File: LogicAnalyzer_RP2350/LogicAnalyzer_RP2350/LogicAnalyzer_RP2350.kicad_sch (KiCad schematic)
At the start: 0 parts

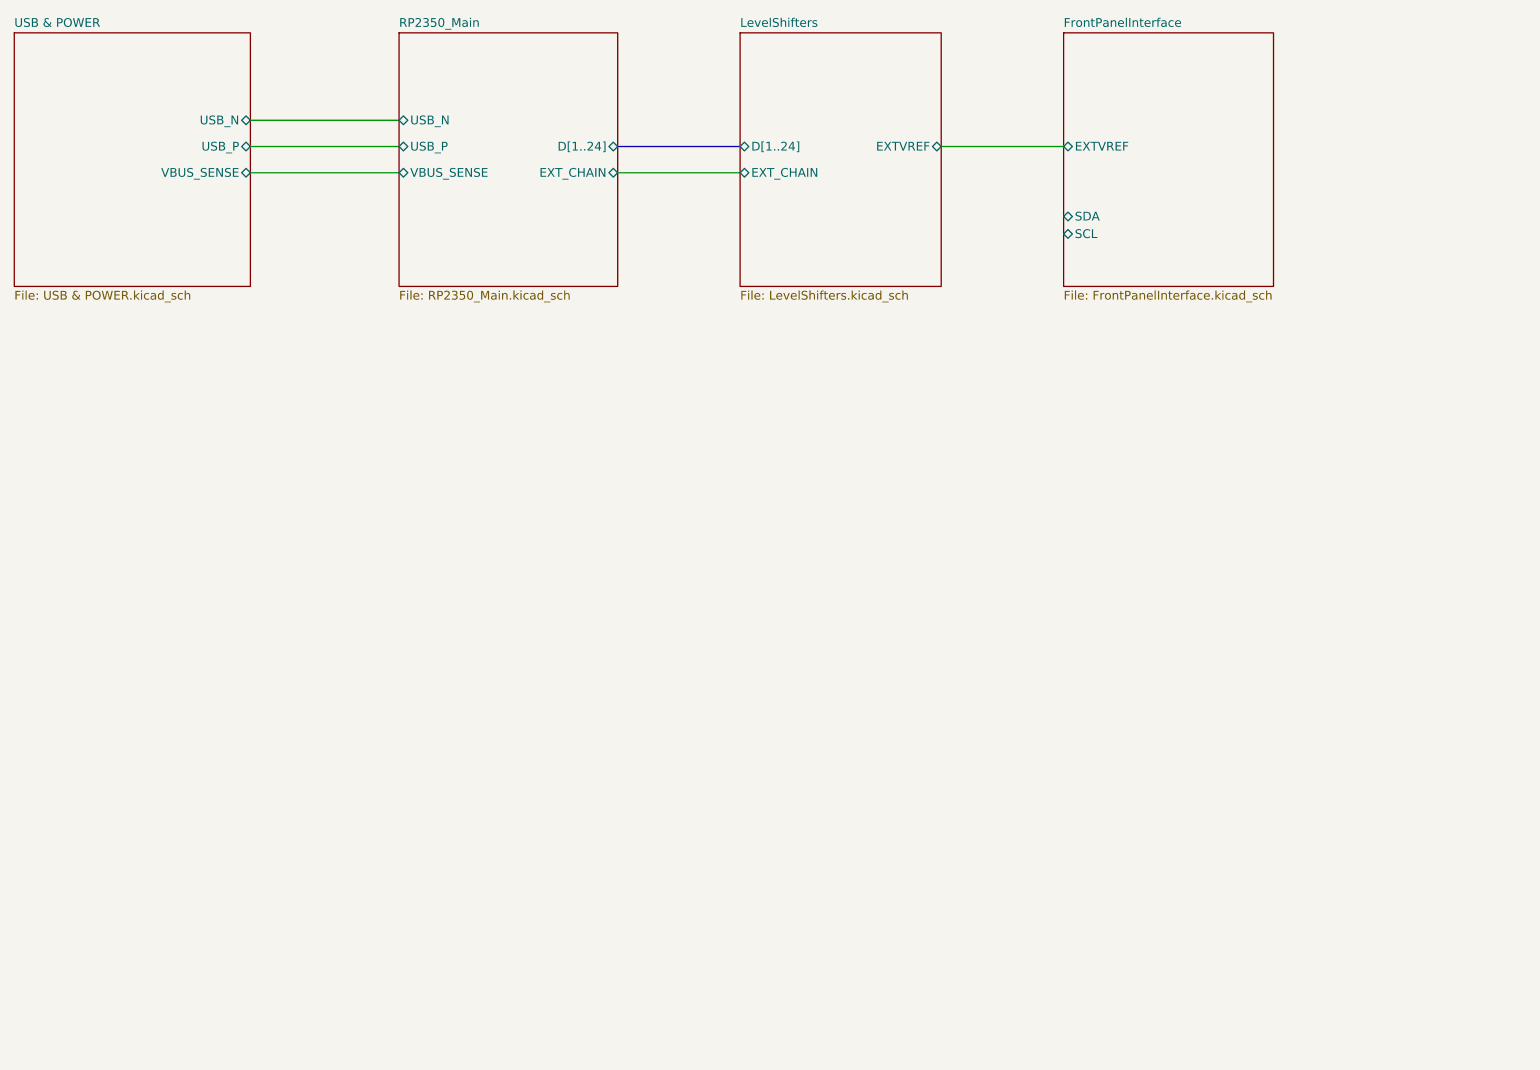
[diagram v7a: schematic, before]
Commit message: Clearing UP ERC Errors and Warnings
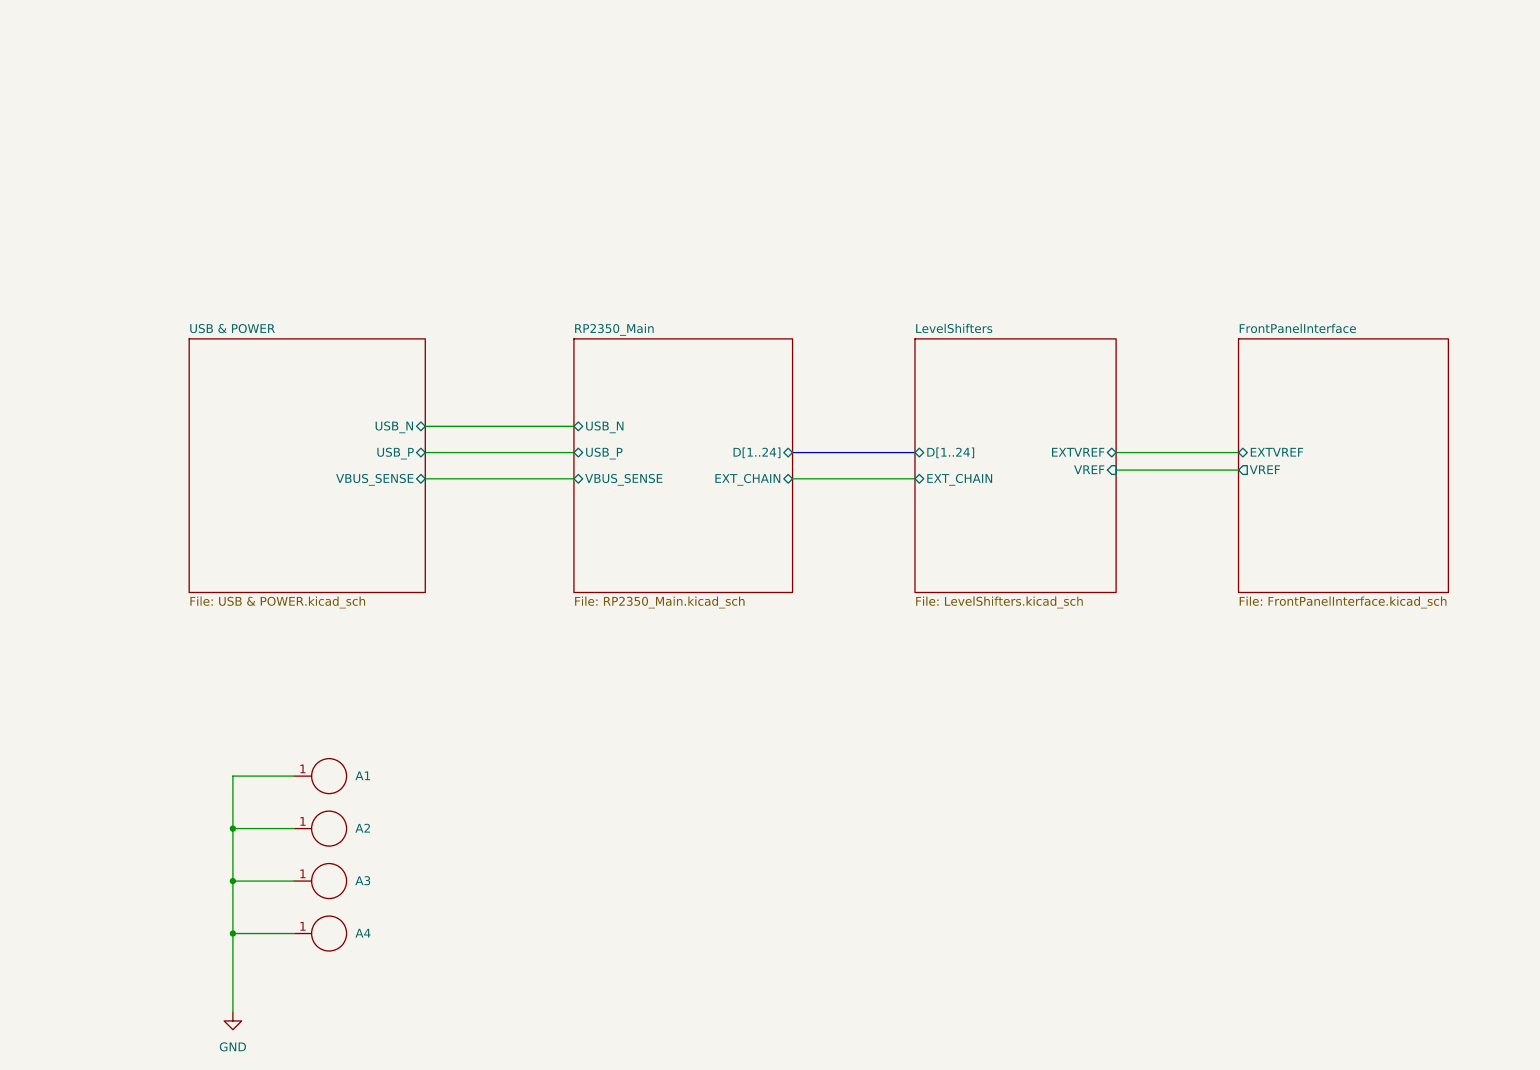
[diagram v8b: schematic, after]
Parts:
- added A1, A2, A3, A4: 9774050151R, Assembly_SMD_Wurth:A_Wurth_WA-SMSI_9774050151R, symbol Assembly_Wurth_WA-SMSI:9774050151R
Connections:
- new net GND: A1.1, A2.1, A3.1, A4.1
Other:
- sheet FrontPanelInterface ports: added VREF; removed SCL, SDA
- sheet LevelShifters ports: added VREF; removed none
